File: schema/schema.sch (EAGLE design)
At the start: 18 parts

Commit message: Small changes in the eagle schema
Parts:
- removed D1: BZX85C3V3, diode:BZX85
- added BZX85C3V3: D1, diode:BZX85
- added R3: 30K, resistor:R-EU_0207/10
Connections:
- net 3V3: now also R3.2
- net N$4: now also BZX85C3V3.A, R3.1; no longer D1.A
- net XBEE: now also BZX85C3V3.C; no longer D1.C
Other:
- moved on the sheet: C6
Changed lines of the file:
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@@
 <part name="C5" library="rcl" deviceset="C-EU" device="025-025X050" value="22pF"/>
 <part name="C6" library="rcl" deviceset="C-EU" device="025-025X050" value="330nF"/>
-<part name="D1" library="diode" deviceset="BZX85" device="" value="BZX85C3V3"/>
+<part name="BZX85C3V3" library="diode" deviceset="BZX85" device="" value="D1"/>
 <part name="R1" library="resistor" deviceset="R-EU_" device="0207/10" value="10K"/>
 <part name="R2" library="resistor" deviceset="R-EU_" device="0207/10" value="10K"/>
 <part name="LED1" library="led" deviceset="LED" device="3MM"/>
+<part name="R3" library="resistor" deviceset="R-EU_" device="0207/10" value="30K"/>
 </parts>
 <sheets>
@@
 <instance part="C4" gate="G$1" x="15.24" y="58.42" rot="R90"/>
 <instance part="C5" gate="G$1" x="15.24" y="48.26" rot="R90"/>
-<instance part="C6" gate="G$1" x="170.18" y="40.64"/>
-<instance part="D1" gate="D" x="129.54" y="76.2" rot="R180"/>
+<instance part="C6" gate="G$1" x="170.18" y="38.1"/>
+<instance part="BZX85C3V3" gate="D" x="121.92" y="71.12" rot="R180"/>
 <instance part="R1" gate="G$1" x="27.94" y="91.44" rot="R90"/>
 <instance part="R2" gate="G$1" x="109.22" y="45.72" rot="R90"/>
 <instance part="LED1" gate="G$1" x="109.22" y="35.56"/>
+<instance part="R3" gate="G$1" x="129.54" y="76.2" rot="R90"/>
 </instances>
 <busses>
@@
 <pinref part="C6" gate="G$1" pin="2"/>
 <wire x1="149.86" y1="30.48" x2="149.86" y2="25.4" width="0.2032" layer="91"/>
-<wire x1="170.18" y1="35.56" x2="170.18" y2="30.48" width="0.2032" layer="91"/>
+<wire x1="170.18" y1="33.02" x2="170.18" y2="30.48" width="0.2032" layer="91"/>
 <wire x1="170.18" y1="30.48" x2="149.86" y2="30.48" width="0.2032" layer="91"/>
 <label x="149.86" y="25.4" size="1.778" layer="95"/>
+<junction x="149.86" y="30.48"/>
 </segment>
 <segment>
@@
 <net name="3V3" class="0">
 <segment>
-<pinref part="REGULATOR" gate="G$1" pin="O"/>
-<wire x1="160.02" y1="43.18" x2="170.18" y2="43.18" width="0.2032" layer="91"/>
-<label x="177.8" y="43.18" size="1.778" layer="95"/>
-<pinref part="C6" gate="G$1" pin="1"/>
-<wire x1="170.18" y1="43.18" x2="177.8" y2="43.18" width="0.2032" layer="91"/>
-<junction x="170.18" y="43.18"/>
-</segment>
-<segment>
 <pinref part="RADIO" gate="G$1" pin="VDD"/>
 <wire x1="137.16" y1="81.28" x2="129.54" y2="81.28" width="0.2032" layer="91"/>
-<label x="129.54" y="81.28" size="1.778" layer="95"/>
+<label x="121.92" y="81.28" size="1.778" layer="95"/>
+<pinref part="R3" gate="G$1" pin="2"/>
+<wire x1="129.54" y1="81.28" x2="121.92" y2="81.28" width="0.2032" layer="91"/>
+<junction x="129.54" y="81.28"/>
 </segment>
 <segment>
@@
 <label x="124.46" y="43.18" size="1.778" layer="95"/>
 </segment>
-</net>
-<net name="N$4" class="0">
-<segment>
-<pinref part="RADIO" gate="G$1" pin="DIN"/>
-<pinref part="D1" gate="D" pin="A"/>
-<wire x1="137.16" y1="76.2" x2="132.08" y2="76.2" width="0.2032" layer="91"/>
+<segment>
+<pinref part="REGULATOR" gate="G$1" pin="O"/>
+<wire x1="160.02" y1="43.18" x2="170.18" y2="43.18" width="0.2032" layer="91"/>
+<pinref part="C6" gate="G$1" pin="1"/>
+<wire x1="170.18" y1="43.18" x2="175.26" y2="43.18" width="0.2032" layer="91"/>
+<wire x1="170.18" y1="40.64" x2="170.18" y2="43.18" width="0.2032" layer="91"/>
+<junction x="170.18" y="43.18"/>
+<label x="175.26" y="43.18" size="1.778" layer="95"/>
 </segment>
 </net>
 <net name="XBEE" class="0">
 <segment>
-<pinref part="D1" gate="D" pin="C"/>
-<wire x1="127" y1="76.2" x2="109.22" y2="76.2" width="0.2032" layer="91"/>
-<label x="109.22" y="76.2" size="1.778" layer="95"/>
+<pinref part="BZX85C3V3" gate="D" pin="C"/>
+<wire x1="119.38" y1="71.12" x2="111.76" y2="71.12" width="0.2032" layer="91"/>
+<label x="111.76" y="71.12" size="1.778" layer="95"/>
 </segment>
 <segment>
@@
 </segment>
 </net>
+<net name="N$4" class="0">
+<segment>
+<pinref part="RADIO" gate="G$1" pin="DIN"/>
+<wire x1="137.16" y1="76.2" x2="134.62" y2="76.2" width="0.2032" layer="91"/>
+<wire x1="134.62" y1="76.2" x2="134.62" y2="71.12" width="0.2032" layer="91"/>
+<pinref part="BZX85C3V3" gate="D" pin="A"/>
+<wire x1="134.62" y1="71.12" x2="129.54" y2="71.12" width="0.2032" layer="91"/>
+<pinref part="R3" gate="G$1" pin="1"/>
+<junction x="129.54" y="71.12"/>
+<wire x1="129.54" y1="71.12" x2="124.46" y2="71.12" width="0.2032" layer="91"/>
+</segment>
+</net>

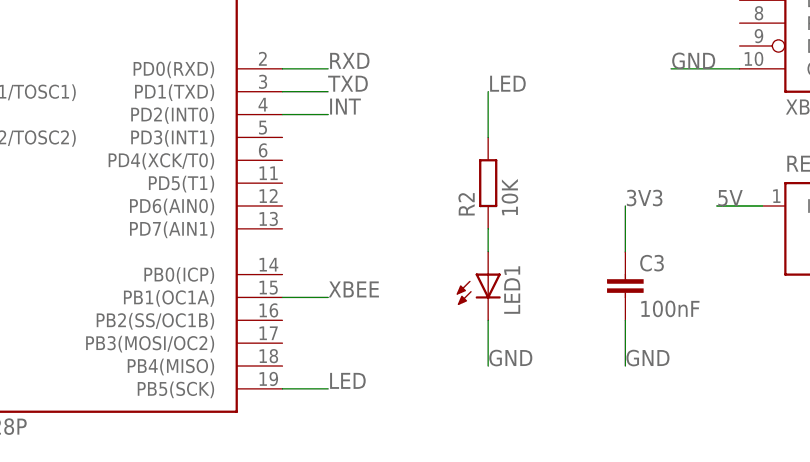
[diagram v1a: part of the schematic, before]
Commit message: Stripboard design and PIN changes
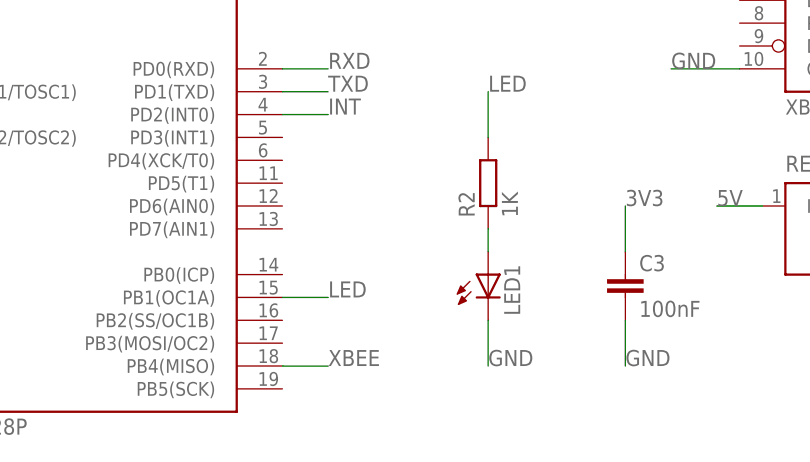
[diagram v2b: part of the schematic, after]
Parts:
- R2: value 10K -> 1K
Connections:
- net LED: now also MUC.PB1(OC1A); no longer MUC.PB5(SCK)
- net XBEE: now also MUC.PB4(MISO); no longer MUC.PB1(OC1A)
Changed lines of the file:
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@@
 <part name="BZX85C3V3" library="diode" deviceset="BZX85" device="" value="D1"/>
 <part name="R1" library="resistor" deviceset="R-EU_" device="0207/10" value="10K"/>
-<part name="R2" library="resistor" deviceset="R-EU_" device="0207/10" value="10K"/>
+<part name="R2" library="resistor" deviceset="R-EU_" device="0207/10" value="1K"/>
 <part name="LED1" library="led" deviceset="LED" device="3MM"/>
 <part name="R3" library="resistor" deviceset="R-EU_" device="0207/10" value="30K"/>
@@
 </segment>
 <segment>
-<pinref part="MUC" gate="G$1" pin="PB1(OC1A)"/>
-<wire x1="86.36" y1="33.02" x2="91.44" y2="33.02" width="0.2032" layer="91"/>
-<label x="91.44" y="33.02" size="1.778" layer="95"/>
+<pinref part="MUC" gate="G$1" pin="PB4(MISO)"/>
+<wire x1="86.36" y1="25.4" x2="91.44" y2="25.4" width="0.1524" layer="91"/>
+<label x="91.44" y="25.4" size="1.778" layer="95"/>
 </segment>
 </net>
 <net name="LED" class="0">
-<segment>
-<pinref part="MUC" gate="G$1" pin="PB5(SCK)"/>
-<wire x1="86.36" y1="22.86" x2="91.44" y2="22.86" width="0.2032" layer="91"/>
-<label x="91.44" y="22.86" size="1.778" layer="95"/>
-</segment>
 <segment>
 <pinref part="R2" gate="G$1" pin="2"/>
@@
 <label x="109.22" y="55.88" size="1.778" layer="95"/>
 </segment>
-</net>
+<segment>
+<pinref part="MUC" gate="G$1" pin="PB1(OC1A)"/>
+<wire x1="86.36" y1="33.02" x2="91.44" y2="33.02" width="0.1524" layer="91"/>
+<label x="91.44" y="33.02" size="1.778" layer="95"/>
+</segment>
+</net>

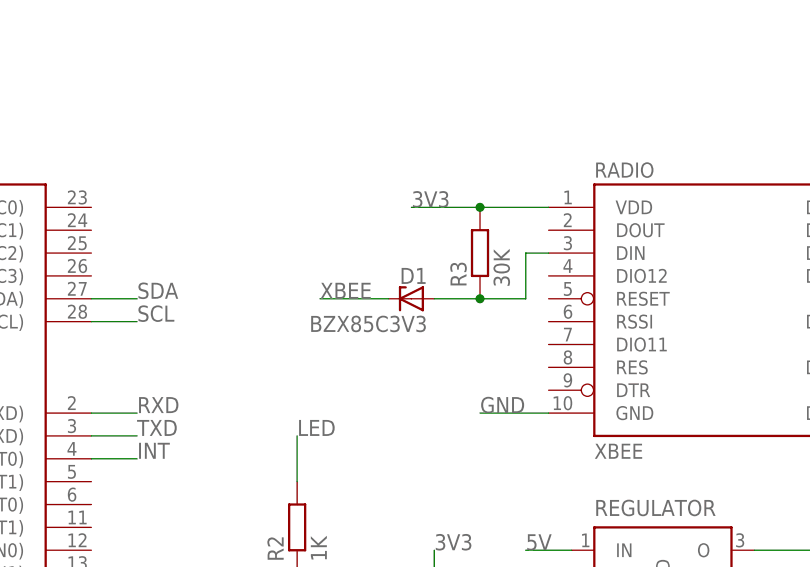
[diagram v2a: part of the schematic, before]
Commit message: Bug fix in the eagle schema: replace zener for schottky
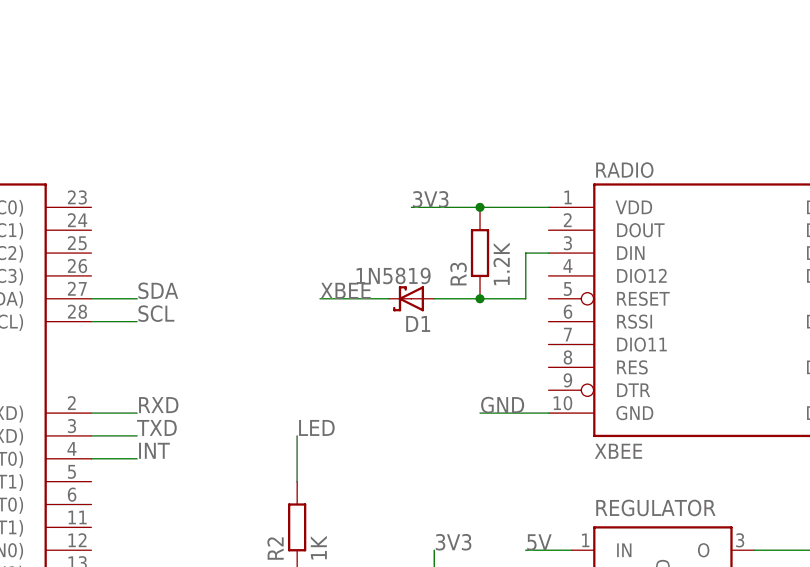
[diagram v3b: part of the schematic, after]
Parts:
- removed BZX85C3V3: D1, diode:BZX85
- added D1: 1N5819, diode:1N5819-B
- R3: value 30K -> 1.2K
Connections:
- net N$4: now also D1.A; no longer BZX85C3V3.A
- net XBEE: now also D1.C; no longer BZX85C3V3.C
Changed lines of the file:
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@@
 <part name="C5" library="rcl" deviceset="C-EU" device="025-025X050" value="22pF"/>
 <part name="C6" library="rcl" deviceset="C-EU" device="025-025X050" value="330nF"/>
-<part name="BZX85C3V3" library="diode" deviceset="BZX85" device="" value="D1"/>
 <part name="R1" library="resistor" deviceset="R-EU_" device="0207/10" value="10K"/>
 <part name="R2" library="resistor" deviceset="R-EU_" device="0207/10" value="1K"/>
 <part name="LED1" library="led" deviceset="LED" device="3MM"/>
-<part name="R3" library="resistor" deviceset="R-EU_" device="0207/10" value="30K"/>
+<part name="R3" library="resistor" deviceset="R-EU_" device="0207/10" value="1.2K"/>
+<part name="D1" library="diode" deviceset="1N581*" device="" technology="9-B" value="1N5819"/>
 </parts>
 <sheets>
@@
 <instance part="C5" gate="G$1" x="15.24" y="48.26" rot="R90"/>
 <instance part="C6" gate="G$1" x="170.18" y="38.1"/>
-<instance part="BZX85C3V3" gate="D" x="121.92" y="71.12" rot="R180"/>
 <instance part="R1" gate="G$1" x="27.94" y="91.44" rot="R90"/>
 <instance part="R2" gate="G$1" x="109.22" y="45.72" rot="R90"/>
 <instance part="LED1" gate="G$1" x="109.22" y="35.56"/>
 <instance part="R3" gate="G$1" x="129.54" y="76.2" rot="R90"/>
+<instance part="D1" gate="G$1" x="121.92" y="71.12" rot="R180"/>
 </instances>
 <busses>
@@
 <net name="XBEE" class="0">
 <segment>
-<pinref part="BZX85C3V3" gate="D" pin="C"/>
 <wire x1="119.38" y1="71.12" x2="111.76" y2="71.12" width="0.2032" layer="91"/>
 <label x="111.76" y="71.12" size="1.778" layer="95"/>
+<pinref part="D1" gate="G$1" pin="C"/>
 </segment>
 <segment>
@@
 <wire x1="137.16" y1="76.2" x2="134.62" y2="76.2" width="0.2032" layer="91"/>
 <wire x1="134.62" y1="76.2" x2="134.62" y2="71.12" width="0.2032" layer="91"/>
-<pinref part="BZX85C3V3" gate="D" pin="A"/>
 <wire x1="134.62" y1="71.12" x2="129.54" y2="71.12" width="0.2032" layer="91"/>
 <pinref part="R3" gate="G$1" pin="1"/>
 <junction x="129.54" y="71.12"/>
 <wire x1="129.54" y1="71.12" x2="124.46" y2="71.12" width="0.2032" layer="91"/>
-</segment>
-</net>
+<pinref part="D1" gate="G$1" pin="A"/>
+</segment>
+</net>

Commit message: Fix schematics
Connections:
- net RXD: now also FTDI.4; no longer FTDI.5
- net TXD: now also FTDI.5; no longer FTDI.4
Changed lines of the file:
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@@
 <net name="TXD" class="0">
+<segment>
+<pinref part="MUC" gate="G$1" pin="PD1(TXD)"/>
+<wire x1="86.36" y1="55.88" x2="91.44" y2="55.88" width="0.2032" layer="91"/>
+<label x="91.44" y="55.88" size="1.778" layer="95"/>
+</segment>
+<segment>
+<pinref part="FTDI" gate="G$1" pin="5"/>
+<wire x1="-15.24" y1="78.74" x2="-10.16" y2="78.74" width="0.2032" layer="91"/>
+<label x="-10.16" y="78.74" size="1.778" layer="95"/>
+</segment>
+</net>
+<net name="RXD" class="0">
+<segment>
+<pinref part="MUC" gate="G$1" pin="PD0(RXD)"/>
+<wire x1="86.36" y1="58.42" x2="91.44" y2="58.42" width="0.2032" layer="91"/>
+<label x="91.44" y="58.42" size="1.778" layer="95"/>
+</segment>
 <segment>
 <pinref part="FTDI" gate="G$1" pin="4"/>
@@
 <label x="-10.16" y="76.2" size="1.778" layer="95"/>
 </segment>
-<segment>
-<pinref part="MUC" gate="G$1" pin="PD1(TXD)"/>
-<wire x1="86.36" y1="55.88" x2="91.44" y2="55.88" width="0.2032" layer="91"/>
-<label x="91.44" y="55.88" size="1.778" layer="95"/>
-</segment>
 </net>
-<net name="RXD" class="0">
-<segment>
-<pinref part="FTDI" gate="G$1" pin="5"/>
-<wire x1="-15.24" y1="78.74" x2="-10.16" y2="78.74" width="0.2032" layer="91"/>
-<label x="-10.16" y="78.74" size="1.778" layer="95"/>
-</segment>
-<segment>
-<pinref part="MUC" gate="G$1" pin="PD0(RXD)"/>
-<wire x1="86.36" y1="58.42" x2="91.44" y2="58.42" width="0.2032" layer="91"/>
-<label x="91.44" y="58.42" size="1.778" layer="95"/>
-</segment>
-</net>
